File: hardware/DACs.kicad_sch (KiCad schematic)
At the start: 70 parts, among them U10 LT1678CS8#PBF, U11 LT1678CS8#PBF, U12 LT1678CS8#PBF, U13 LT1678CS8#PBF, U14 LT1461CIS8-2.5#PBF, U6 LTC2642ACDD-16#PBF, U7 LTC2642ACDD-16#PBF, U8 LTC2642ACDD-16#PBF, U9 LTC2642ACDD-16#PBF

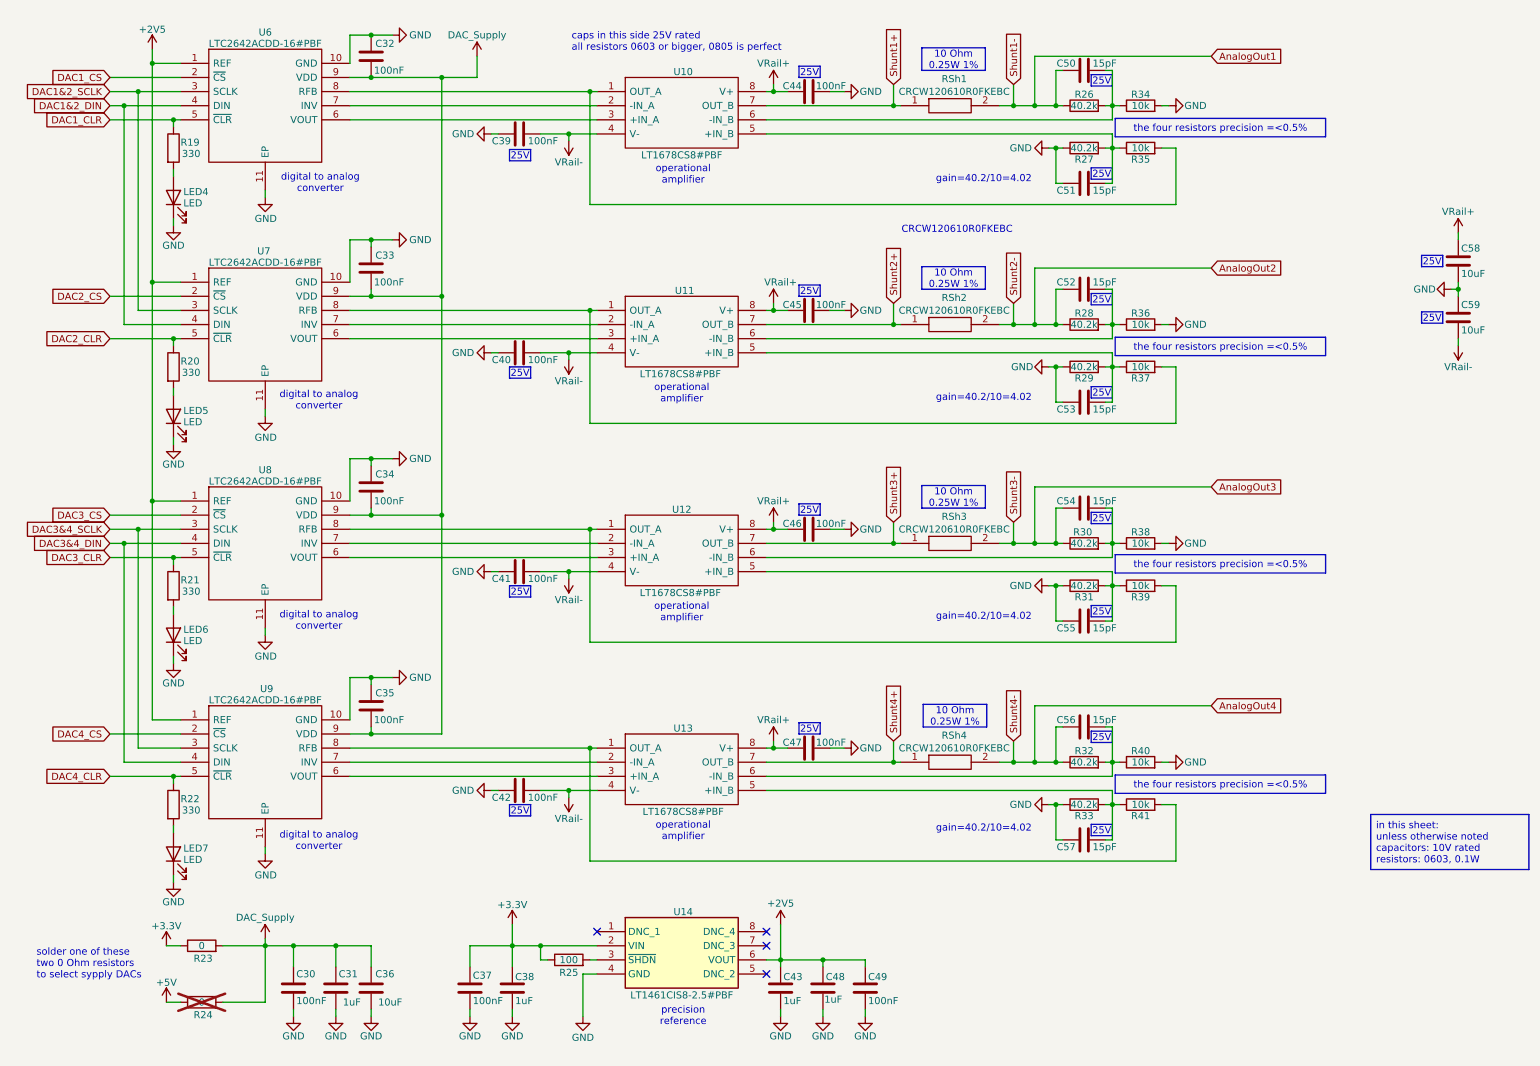
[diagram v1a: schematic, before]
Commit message: BOM for all capacitors and resistors is added correctly to the schematic
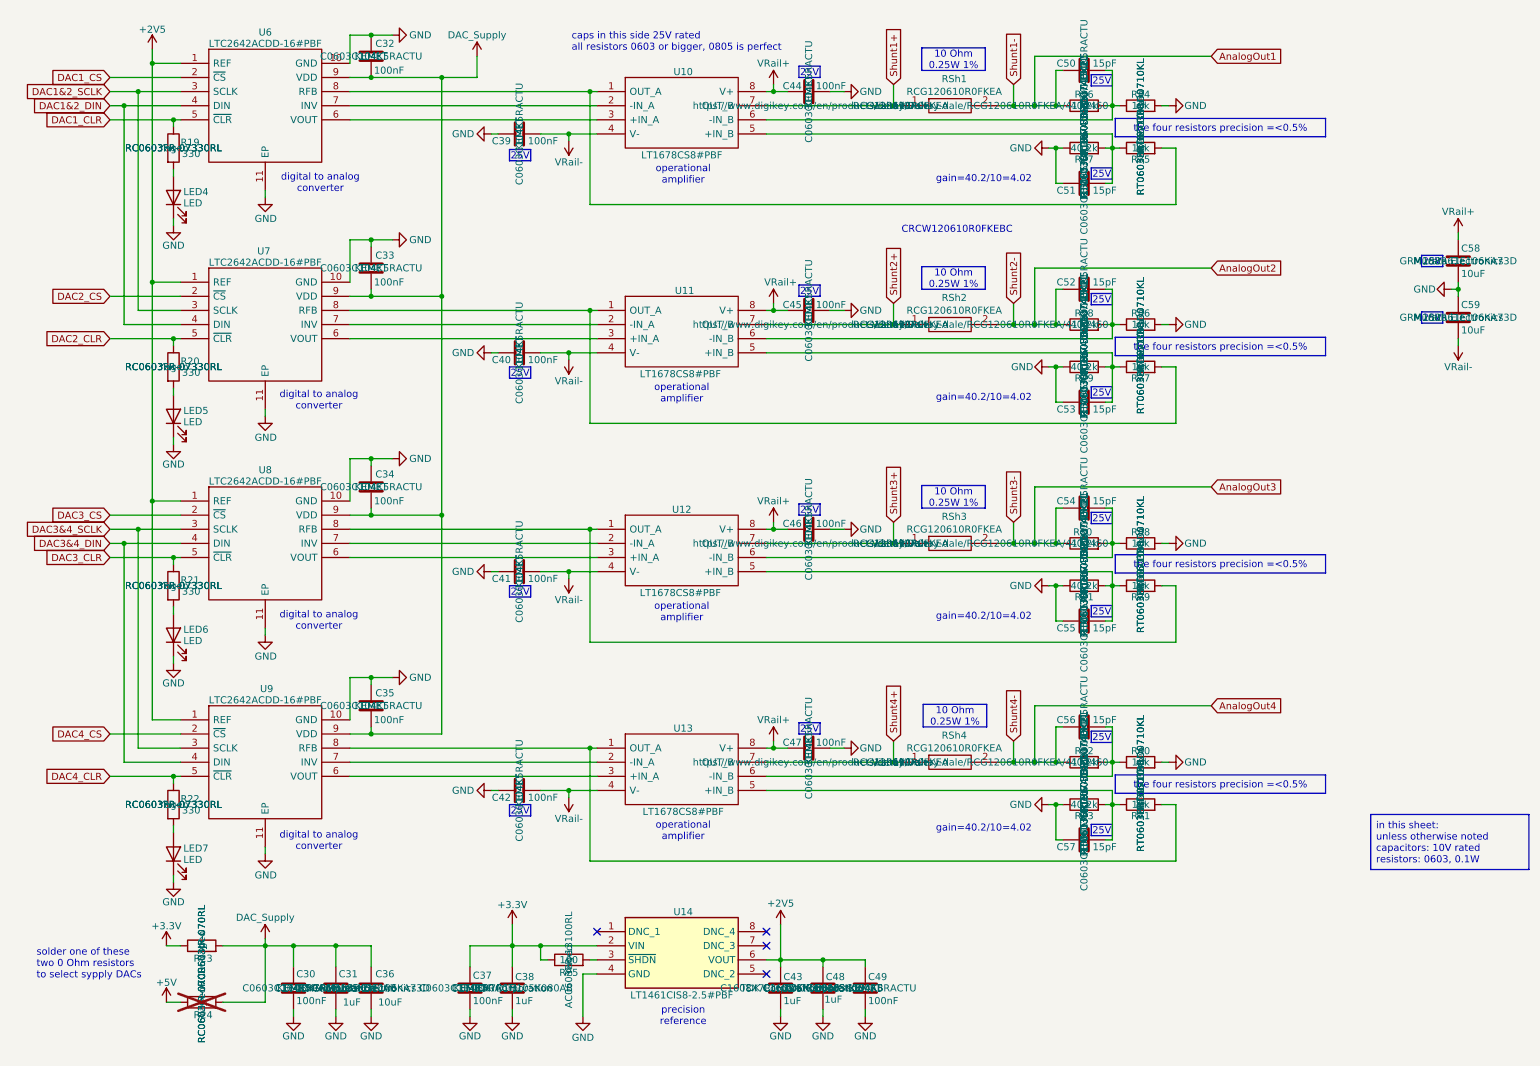
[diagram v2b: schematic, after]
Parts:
- C30, C32, C33, C34, C35, C37, C39, C40, C41, C42, C44, C45, C46, C47, C49: Link https://www.digikey.com/en/products/detail/walsin-technolog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 -> https://www.digikey.com/en/products/detail/kemet/C0603C104K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; MPN (none) -> C0603C104K5RACTU; Manufacturer Walson Technology Corporation -> KEMET; Manufacturer Number 0402B104K160CT -> (none); Manufacturer_Name (none) -> KEMET; Manufacturer_Part_Number (none) -> C0603C104K5RACTU; Rated Voltage 16V -> 50V
- C31, C38, C43, C48: Link https://www.digikey.com/en/products/detail/murata-electroni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 -> https://www.digikey.com/en/products/detail/tdk-corporation/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; MPN (none) -> C1608X7R1H105K080AB; Manufacturer Murata Electronics -> TDK Corporation; Manufacturer Number GRM155R6YA105KE11J -> (none); Manufacturer_Name (none) -> TDK Corporation; Manufacturer_Part_Number (none) -> C1608X7R1H105K080AB; Rated Voltage 35V -> 50V; Tolerance (none) -> 10%
- C36, C58, C59: Link https://www.digikey.com/en/products/detail/murata-electronics/GRM21BZ71E106KE15L/13904911 -> https://www.digikey.com/en/products/detail/murata-electronics/GRM188R61E106KA73D/9867922; MPN (none) -> GRM188R61E106KA73D; Manufacturer Number GRM21BZ71E106KE15L -> (none); Manufacturer_Name (none) -> Murata Electronics; Manufacturer_Part_Number (none) -> GRM188R61E106KA73D; Tolerance (none) -> 10%
- C50, C51, C52, C53, C54, C55, C56, C57: Link https://www.digikey.com/en/products/detail/walsin-technolog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 -> https://www.digikey.com/en/products/detail/kemet/C0603C150K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; MPN (none) -> C0603C150K5RACTU; Manufacturer Walson Technology Corporation -> KEMET; Manufacturer Number 0402B104K160CT -> (none); Manufacturer_Name (none) -> KEMET; Manufacturer_Part_Number (none) -> C0603C150K5RACTU; Rated Voltage 16V -> 50V
- R19, R20, R21, R22: Link https://www.digikey.com/en/products/detail/yageo/RC0402FR-0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 -> https://www.digikey.com/en/products/detail/yageo/RC0603FR-0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; MPN (none) -> RC0603FR-07330RL; Manufacturer_Name (none) -> Yageo; Manufacturer_Part_Number (none) -> RC0603FR-07330RL
- R23, R24: Link https://www.digikey.com/en/products/detail/yageo/RT0402BRD0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 -> https://www.digikey.com/en/products/detail/yageo/RC0603JR-0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; MPN (none) -> RC0603JR-070RL; Manufacturer_Name (none) -> Yageo; Manufacturer_Part_Number (none) -> RC0603JR-070RL; Tolerance 1% -> (none)
- R25: Link https://www.digikey.com/en/products/detail/yageo/RT0402BRD0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 -> https://www.digikey.com/en/products/detail/yageo/AC0603FR-1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; MPN (none) -> AC0603FR-13100RL; Manufacturer_Name (none) -> Yageo; Manufacturer_Part_Number (none) -> AC0603FR-13100RL
- R26, R27, R28, R29, R30, R31, R32, R33: Link https://www.digikey.com/en/products/detail/yageo/RT0402BRD0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 -> https://www.digikey.com/en/products/detail/yageo/RT0603BRD0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; MPN (none) -> RT0603BRD0740K2L; Manufacturer_Name (none) -> Yageo; Manufacturer_Part_Number (none) -> RT0603BRD0740K2L; Tolerance 1% -> 0.1%
- R34, R35, R36, R37, R38, R39, R40, R41: Link https://www.digikey.com/en/products/detail/yageo/RT0402BRD0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 -> https://www.digikey.com/en/products/detail/yageo/RT0603BRD0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; MPN (none) -> RT0603BRD0710KL; Manufacturer_Name (none) -> Yageo; Manufacturer_Part_Number (none) -> RT0603BRD0710KL; Tolerance 1% -> 0.1%
- RSh1, RSh2, RSh3, RSh4: value CRCW120610R0FKEBC -> RCG120610R0FKEA; Link (none) -> https://www.digikey.com/en/products/detail/vishay-dale/RCG1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; MPN (none) -> RCG120610R0FKEA; Manufacturer (none) -> Vishay Dale; Manufacturer_Name Vishay -> Vishay Dale; Tolerance (none) -> 1%

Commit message: Not necessary text is hidden + BOM on schematic
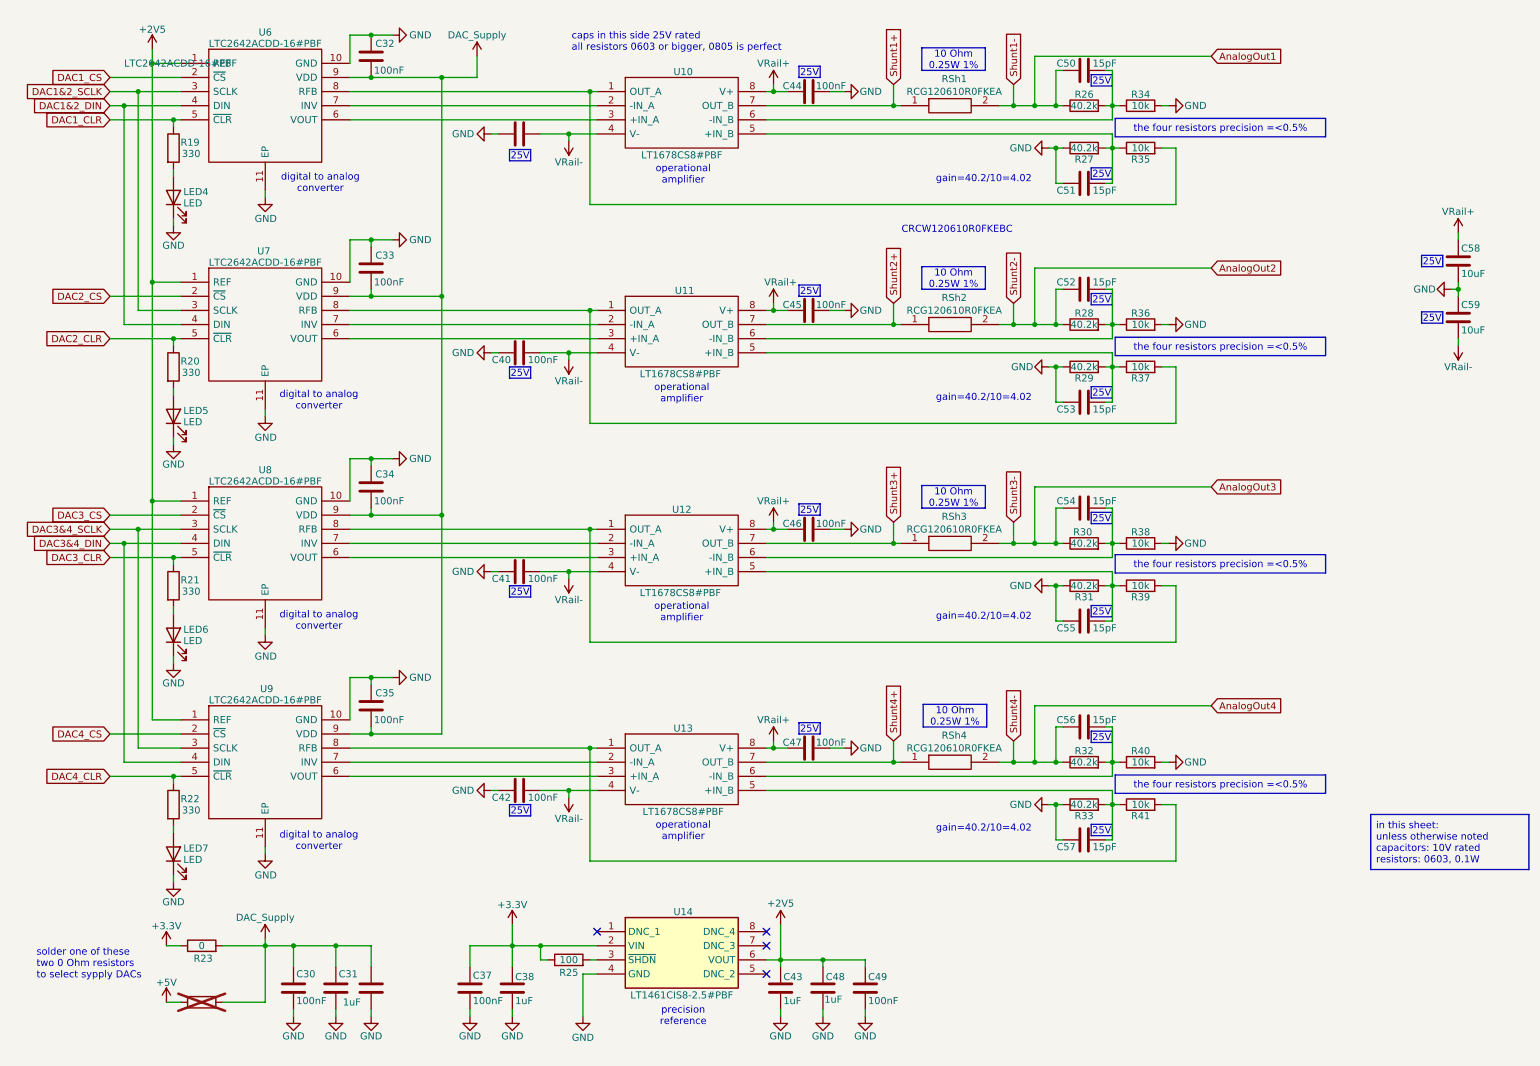
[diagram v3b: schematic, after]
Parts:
- C30, C32, C33, C34, C35, C36, C37, C39, C40, C41, C42, C44, C45, C46, C47, C49, C50, C51, C52, C53, C54, C55, C56, C57, C58, C59: Temperature Coefficient X7R -> (none)
- C31, C38, C43, C48: Temperature Coefficient X5R -> (none)
- LED4, LED5, LED6, LED7: Manufacturer_Part_Number (none) -> XZCDGK53W-1VF
- U10, U11, U12, U13: MPN (none) -> LT1678CS8#PBF
- U14: MPN (none) -> LT1461CIS8-2.5#PBF
- U6, U7, U8, U9: MPN (none) -> LTC2642ACDD-16#PBF

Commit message: Continue BOM + enhance BOM + enhance schematic
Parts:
- C31, C38, C43, C48: Manufacturer TDK Corporation -> TDK; Manufacturer_Name TDK Corporation -> TDK
- LED4, LED5, LED6, LED7: Manufacturer_Name (none) -> SunLED
- U10, U11, U12, U13, U14, U6, U7, U8, U9: Link (none) -> https://www.digikey.com/en/products/detail/analog-devices-i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; Manufacturer (none) -> Analog Devices
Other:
- note added: "Green"
